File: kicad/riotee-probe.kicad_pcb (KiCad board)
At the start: 4 copper layers, 43.2 x 22.9 mm, 72 parts, among them J1 12402012E212A, J2 Conn_01x07, J3 Conn_02x05_Odd_Even, J4 Conn_01x07, U1 RP2040, U2 W25Q16JVUXIQ, U3 74LVC2T45GT, U4 74LVC2T45GT, U5 74LVC2T45GT, U6 74LVC2T45GT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

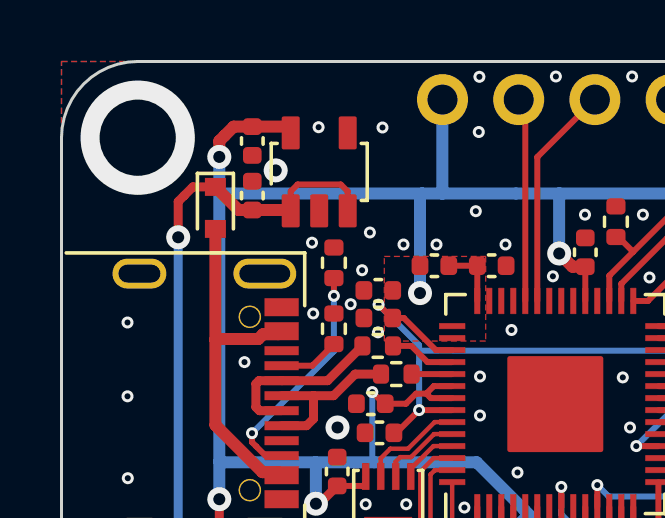
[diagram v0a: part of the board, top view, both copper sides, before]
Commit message: migrate project to kicad 7
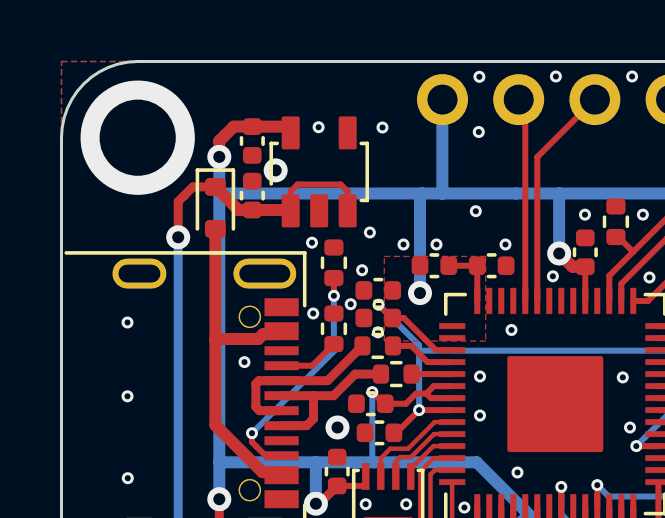
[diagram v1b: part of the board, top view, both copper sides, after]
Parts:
- added REF**: Tab, riotee:KikitTab, F.Cu at (199.4, 50.5)
- added REF**: Tab, riotee:KikitTab, F.Cu at (199.4, 73.9)
